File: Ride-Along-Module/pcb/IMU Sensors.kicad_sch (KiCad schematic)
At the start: 5 parts, among them U3 MS5607-02BA, U4 LSM6DSL

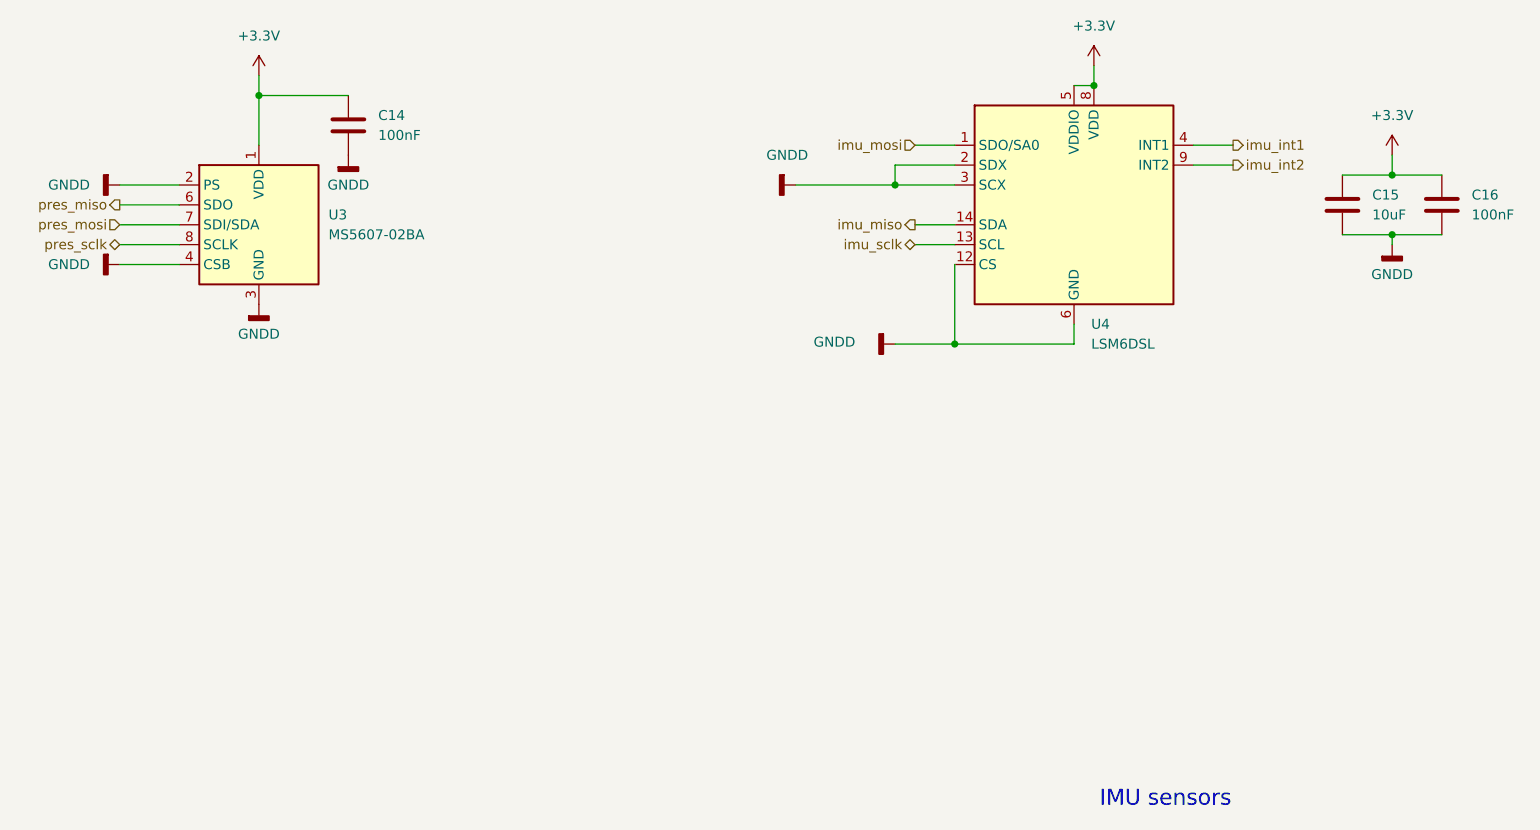
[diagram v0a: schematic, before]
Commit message: More reuse blocks. Added battery circuit to ride along board
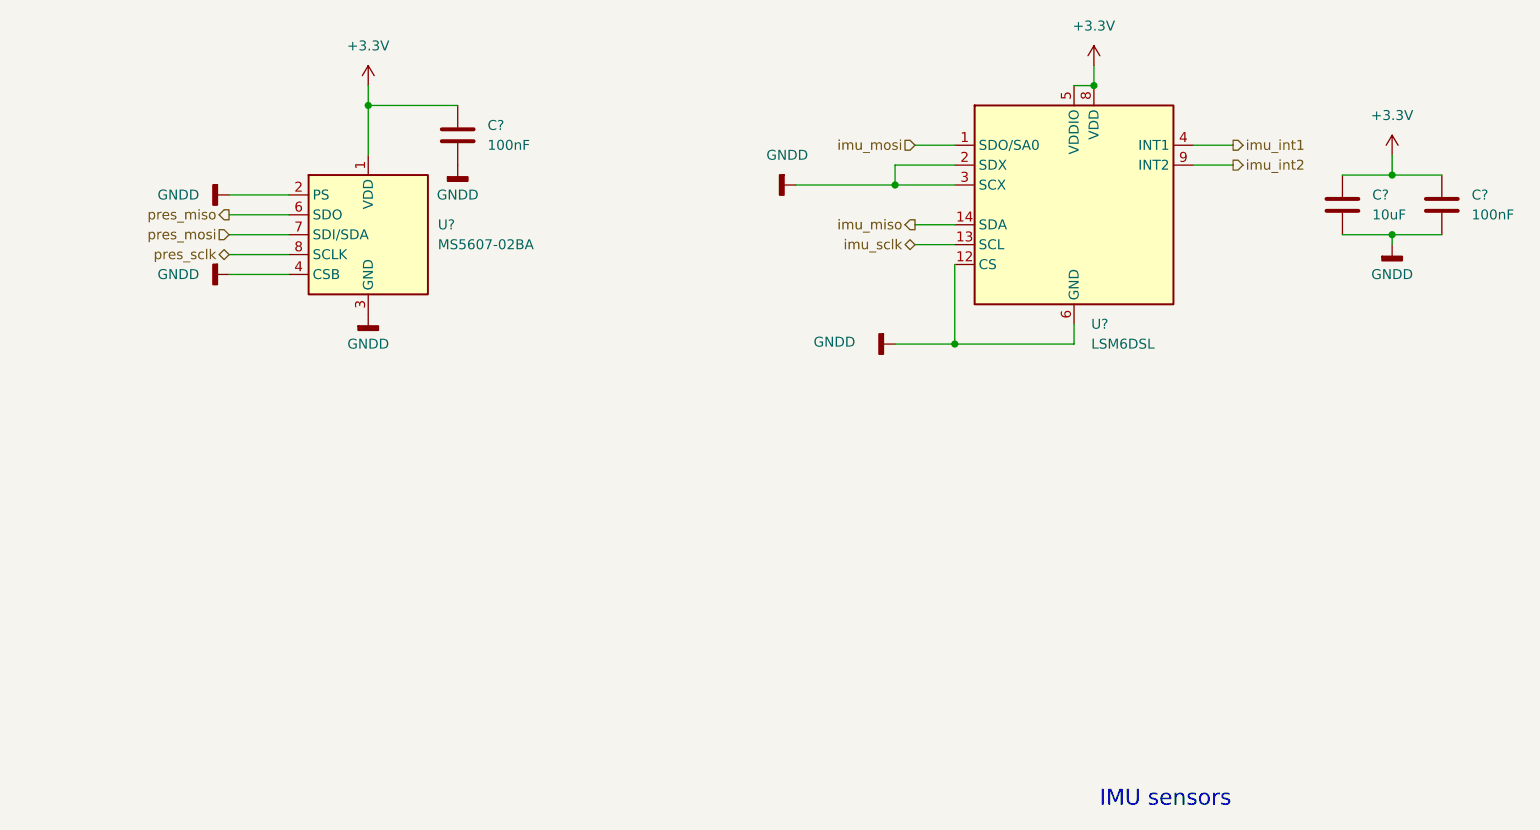
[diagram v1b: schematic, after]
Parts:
- renumbered C14 to C?, C16 to C?, C15 to C?, U3 to U?, U4 to U?
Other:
- moved on the sheet: C?, U?

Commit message: Ride-Along Module Rev. 1
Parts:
- C19, C21: renamed from C?; footprint Capacitor_SMD:C_0603_1608Metric_Pad1.08x0.95mm_HandSolder -> Capacitor_SMD:C_0603_1608Metric
- C20: renamed from C?; footprint Capacitor_Tantalum_SMD:CP_EIA-3216-18_Kemet-A_Pad1.58x1.35mm_HandSolder -> Capacitor_Tantalum_SMD:CP_EIA-3216-18_Kemet-A
- gave numbers to parts that had none: 2
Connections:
- net GNDD: no longer U4.4 (CSB), U4.5 (CSB), U5.12 (CS)
- new net imu_cs: U5.12 (CS)
- new net pres_cs: U4.4 (CSB), U4.5 (CSB)
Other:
- note removed: "IMU sensors"
- company: (none) -> Rowan Rocketry
- title: (none) -> Ride-Along Module
- moved on the sheet: C19, U4
